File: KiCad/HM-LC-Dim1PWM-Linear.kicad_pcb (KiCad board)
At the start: 2 copper layers, 43.2 x 48.8 mm, 16 parts, among them IC1 CC1101, J1 CONN_04, J3 AVR-ISP-10, SW1 Config, U1 L78L05_TO92, U2 PC817, U3 DS18B20

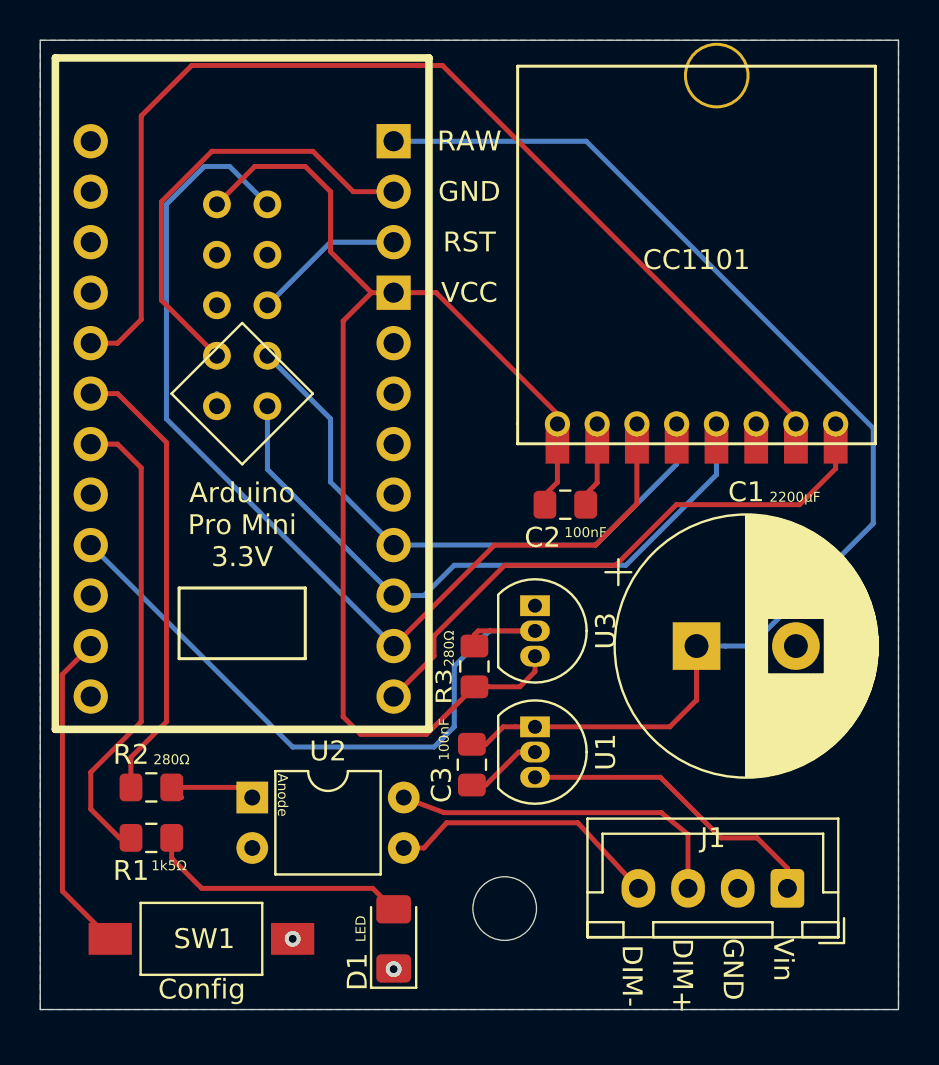
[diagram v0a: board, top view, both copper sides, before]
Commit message: Add R4 PullUp for CC1101
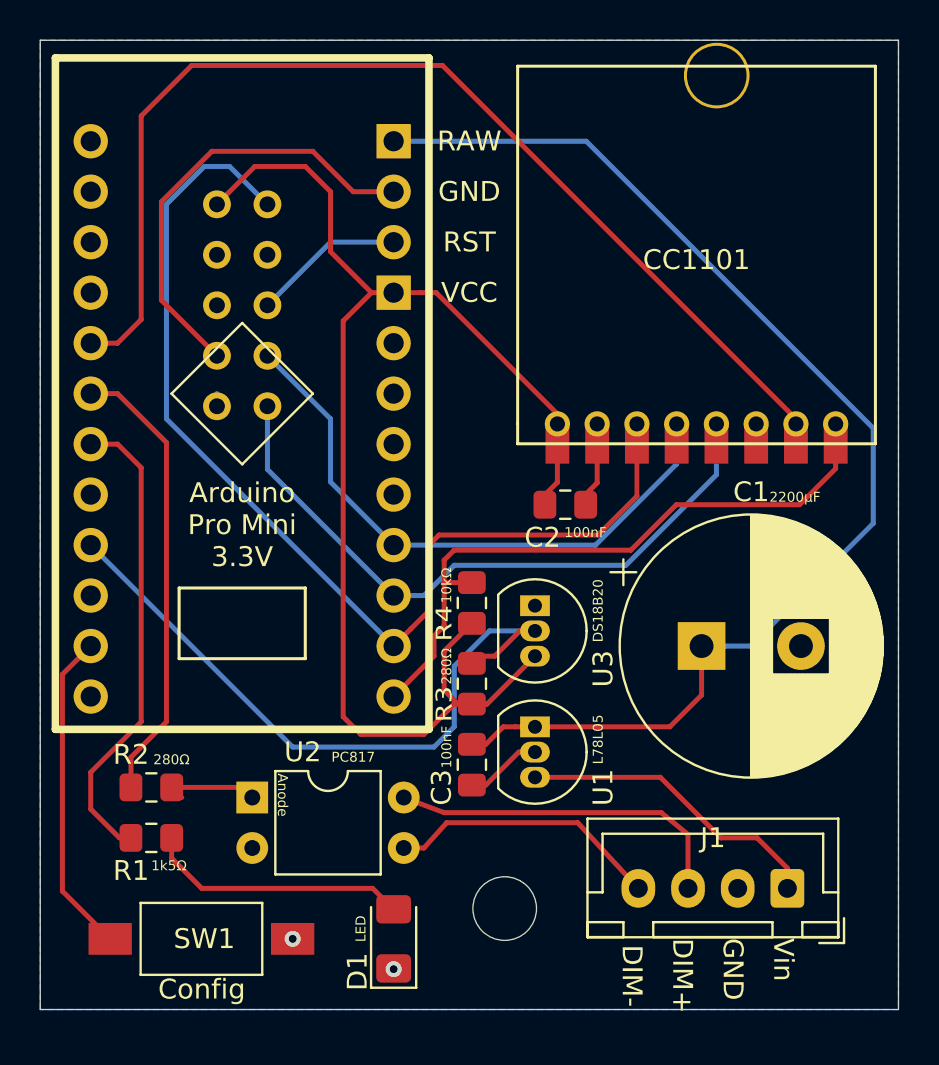
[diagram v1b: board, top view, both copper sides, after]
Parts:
- added R4: 10kΩ, Resistor_SMD:R_0805_2012Metric_Pad1.15x1.40mm_HandSolder, F.Cu at (153.8, 119.8)
- moved R3 0.88 mm to (153.8, 123.8)
- moved C1 0.25 mm to (165.4, 121.9)
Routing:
- net VCC: track 63.2 -> 67.7 mm
- net Net-(B1-Pad13): track 30.4 -> 33.8 mm
- net Net-(B1-Pad14): track 51.8 -> 53.6 mm
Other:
- board text added: "10kΩ"
- board text added: "DS18B20"
- board text added: "HM-LC-Dim1-PWM_Linear v1.2 CC BY-NC-SA 4.0 by Christoph Wiechert"
- board text added: "L78L05"
- board text added: "PC817"
- board text removed: "HM-LC-Dim1-PWM_Linear v1.1 CC BY-NC-SA 4.0 by Christoph Wiechert"
